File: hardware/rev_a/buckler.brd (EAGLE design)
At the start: 63.5 x 125.7 mm, 96 parts, among them J1 DB25_5747846, J2 DM3AT-SF-PEJM5, J3 4P-2.0, J4 4P-2.0, J5 4P-2.0, J6 4P-2.0, J7 4P-2.0, J8 4P-2.0, J9 NRF52840DK_SHIELD, U1 ADXL327, U2 MAX44009, U3 MPU-9250, U4 MS5637-02BA03, U5 SI7021-A20-GM1, U6 SIP32510

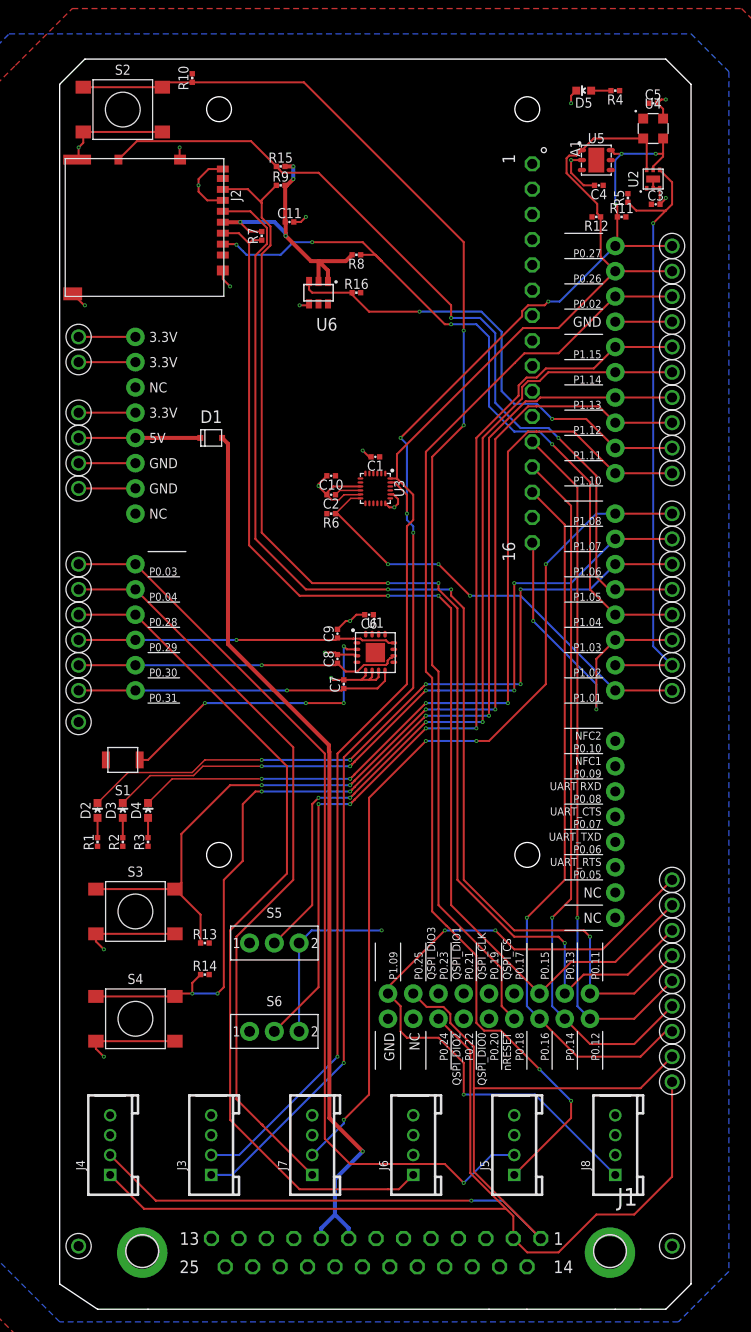
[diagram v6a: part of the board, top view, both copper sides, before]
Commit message: Silkscreen complete
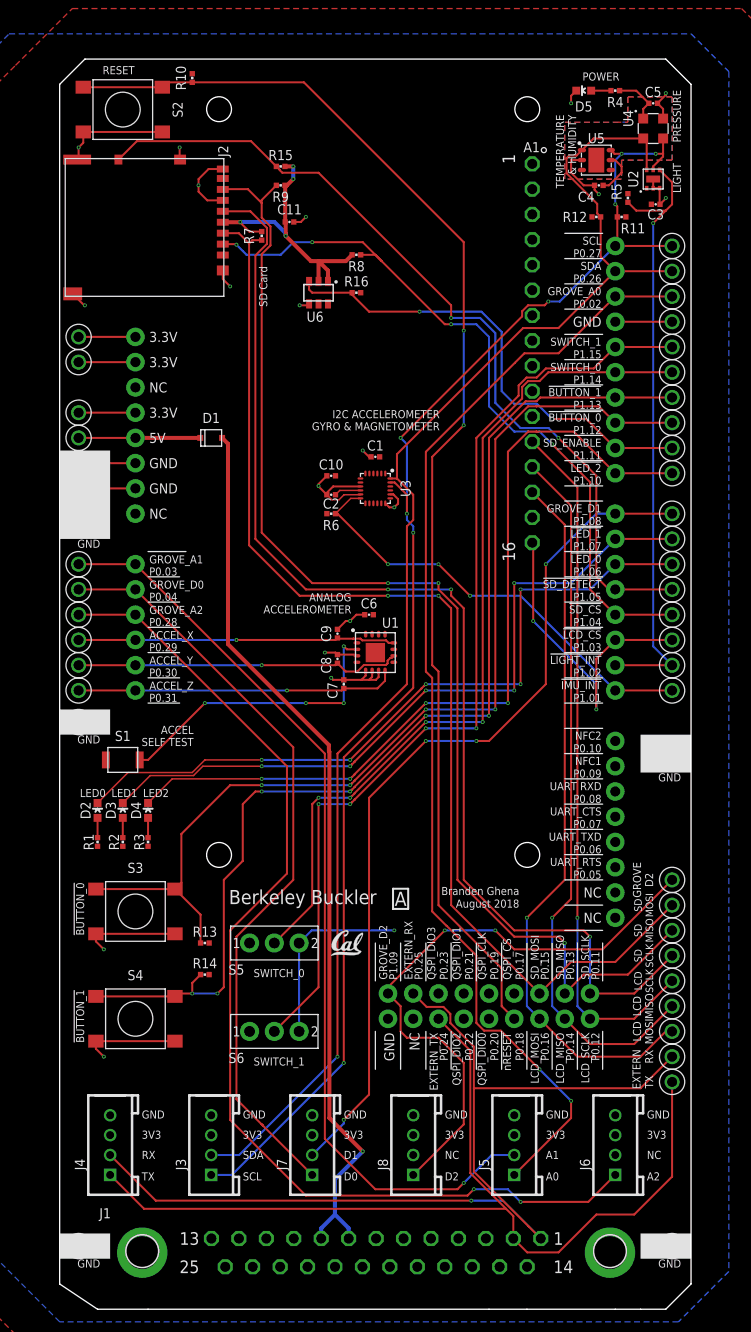
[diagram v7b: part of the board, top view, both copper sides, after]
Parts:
- added TP43, TP44: TEST_POINT_0.078IN, headers:TESTPOINT_0.078IN
- added U$4: (no value), logos:UCB_CAL_100MIL
- moved J6 20.3 mm to (55.9, 10.2)
- moved J8 20.3 mm to (35.6, 10.2)
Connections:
- net GND: now also TP43.1, TP44.1
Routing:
- net GROVE_A2: track 87.1 -> 109.0 mm, vias 0 -> 2
- net +3V3: track 34.9 -> 45.8 mm
- net GROVE_D2: track 69.0 -> 60.6 mm, vias 3 -> 2
- net GND: track 104.3 -> 105.8 mm
- net GROVE_A1: track 93.4 -> 94.0 mm
- added copper zone on layer 1, net N$50
- added copper zone on layer 16, net N$51
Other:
- board text added: "!BUTTON_0"
- board text added: "!BUTTON_1"
- board text added: "!IMU_INT"
- board text added: "!LCD_CS"
- board text added: "!LED_0"
- board text added: "!LED_1"
- board text added: "!LED_2"
- board text added: "!LIGHT_INT"
- board text added: "!SD_CS"
- board text added: "!SD_DETECT"
- board text added: "3V3"
- board text added: "A"
- board text added: "A0"
- board text added: "A1"
- board text added: "A2"
- board text added: "ACCEL SELF TEST"
- board text added: "ACCEL_X"
- board text added: "ACCEL_Y"
- board text added: "ACCEL_Z"
- board text added: "ANALOG ACCELEROMETER"
- board text added: "August 2018"
- board text added: "Berkeley Buckler"
- board text added: "Branden Ghena"
- board text added: "D0"
- board text added: "D1"
- board text added: "D2"
- board text added: "EXTERN"
- board text added: "EXTERN_RX"
- board text added: "EXTERN_TX"
- board text added: "GND"
- board text added: "GROVE D2"
- board text added: "GROVE_A0"
- board text added: "GROVE_A1"
- board text added: "GROVE_A2"
- board text added: "GROVE_D0"
- board text added: "GROVE_D1"
- board text added: "GROVE_D2"
- board text added: "I2C ACCELEROMETER GYRO & MAGNETOMETER"
- board text added: "LCD MISO"
- board text added: "LCD MOSI"
- board text added: "LCD SCLK"
- board text added: "LCD_MISO"
- board text added: "LCD_MOSI"
- board text added: "LCD_SCLK"
- board text added: "LED0"
- board text added: "LED1"
- board text added: "LED2"
- board text added: "LIGHT"
- board text added: "NC"
- board text added: "POWER"
- board text added: "PRESSURE"
- board text added: "RESET"
- board text added: "RX"
- board text added: "SCL"
- board text added: "SD Card"
- board text added: "SD MISO"
- board text added: "SD MOSI"
- board text added: "SD SCLK"
- board text added: "SDA"
- board text added: "SD_ENABLE"
- board text added: "SD_MISO"
- board text added: "SD_MOSI"
- board text added: "SD_SCLK"
- board text added: "SWITCH_0"
- board text added: "SWITCH_1"
- board text added: "TEMPERATURE & HUMIDITY"
- board text added: "TX"

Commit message: Finished with schematic and layout for rev A
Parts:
- C10: value 100nF -> 1uF
- moved C5 58.8 mm to (31.1, 63.5), turned to 180 degrees
- moved D5 49.4 mm to (3.30, 114.7)
- moved C10 42.6 mm to (59.9, 104.8), turned to 0 degrees
- moved R4 32.5 mm to (23.5, 113.0), turned to 270 degrees
- moved C9 15.9 mm to (27.3, 77.5), turned to 180 degrees
- moved R10 10.2 mm to (23.5, 117.5)
- moved C4 9.90 mm to (59.7, 114.9), turned to 0 degrees
- moved C6 7.43 mm to (28.6, 56.5), turned to 90 degrees
- moved C3 6.02 mm to (54.2, 106.7), turned to 180 degrees
- moved C7 2.62 mm to (27.9, 59.1)
- moved C8 2.54 mm to (27.9, 61.6)
- moved S2 1.91 mm to (8.26, 114.3)
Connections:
- net +3V3: now also C9.1; no longer C6.1
- net ANALOG_ACCEL_X: now also C8.1; no longer C9.1
- net ANALOG_ACCEL_Y: now also C7.1; no longer C8.1
- net ANALOG_ACCEL_Z: now also C6.1; no longer C7.1
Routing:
- net N$3: track 1.99 -> 20.5 mm
- net N$1: track 128.0 -> 126.1 mm
- net +3V3: track 45.8 -> 44.4 mm, vias 1 -> 2
- net GND: track 105.8 -> 106.6 mm
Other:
- board text added: "BTN_0"
- board text added: "BTN_1"
